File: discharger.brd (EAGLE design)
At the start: 35.6 x 61 mm, 73 parts, among them U1 BW6101, U10 BW6101, U11 BW6101, U12 BW6101, U2 BW6101, U3 BW6101, U4 BW6101, U5 BW6101, U6 BW6101, U7 BW6101, U8 BW6101, U9 BW6101

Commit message: more layout, update pdf
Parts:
- added C1, C10, C11, C12, C2, C3, C4, C5, C6, C7, C8, C9: 0.1uF, resistor:C0603
- R12, R15, R18, R21, R24, R27, R3, R30, R33, R36, R6, R9: device resistor:R0805W -> resistor:R0603
- moved R24 1.83 mm to (8.64, 36.3), turned to 270 degrees
- moved R15 1.83 mm to (8.64, 22.6), turned to 270 degrees
- moved R18 1.83 mm to (8.64, 27.2), turned to 270 degrees
- moved R6 1.83 mm to (8.64, 8.89), turned to 270 degrees
- moved R9 1.83 mm to (8.64, 13.5), turned to 270 degrees
- moved R3 1.83 mm to (8.64, 4.32), turned to 270 degrees
- moved R12 1.83 mm to (8.64, 18.0), turned to 270 degrees
- moved R21 1.83 mm to (8.64, 31.8), turned to 270 degrees
- moved R27 1.83 mm to (8.64, 40.9), turned to 270 degrees
- moved R30 1.83 mm to (8.64, 45.5), turned to 270 degrees
- moved R33 1.83 mm to (8.64, 50.0), turned to 270 degrees
- moved R36 1.83 mm to (8.64, 54.6), turned to 270 degrees
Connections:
- net B-: now also C1.2
- net B1: now also C1.1, C2.2
- net B10: now also C10.1, C11.2
- net B11: now also C11.1, C12.2
- net B12: now also C12.1
- net B2: now also C2.1, C3.2
- net B3: now also C3.1, C4.2
- net B4: now also C4.1, C5.2
- net B5: now also C5.1, C6.2
- net B6: now also C6.1, C7.2
- net B7: now also C7.1, C8.2
- net B8: now also C8.1, C9.2
- net B9: now also C10.2, C9.1
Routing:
- net B2: track 89.6 -> 104.1 mm
- net B4: track 80.0 -> 94.0 mm
- net B6: track 73.4 -> 83.7 mm
- net B3: track 85.3 -> 94.3 mm
- net B7: track 67.0 -> 76.0 mm
- net B1: track 95.5 -> 104.5 mm
- net B11: track 44.4 -> 53.2 mm
- net B5: track 76.3 -> 85.1 mm
- net B9: track 58.6 -> 67.4 mm
- net B8: track 66.8 -> 73.5 mm
- net B10: track 60.2 -> 63.3 mm
- net B-: track 98.5 -> 101.5 mm
- net B12: track 17.4 -> 14.6 mm, vias 1 -> 0
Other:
- board text added: "B-"
- board text added: "B1"
- board text added: "B10"
- board text added: "B11"
- board text added: "B12"
- board text added: "B2"
- board text added: "B3"
- board text added: "B4"
- board text added: "B5"
- board text added: "B6"
- board text added: "B7"
- board text added: "B8"
- board text added: "B9"
- board text added: "BW6101 Discharger"

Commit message: layout tweaks
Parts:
- LED1, LED10, LED11, LED12, LED2, LED3, LED4, LED5, LED6, LED7, LED8, LED9: device led:CHIP-LED0805 -> led:CHIP-LED0603
- R1, R10, R16, R19, R22, R25, R28, R31, R34, R4, R7: device resistor:R0805W -> resistor:R0603
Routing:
- net N$85: track 2.98 -> 3.48 mm
- net N$75: track 2.98 -> 3.48 mm
- net N$65: track 2.98 -> 3.48 mm
- net N$60: track 2.98 -> 3.48 mm
- net N$50: track 2.98 -> 3.48 mm
- net N$45: track 2.98 -> 3.48 mm
- net N$30: track 2.98 -> 3.48 mm
- net N$25: track 2.98 -> 3.48 mm
- net N$20: track 2.98 -> 3.48 mm
- net N$15: track 2.98 -> 3.48 mm
- net N$10: track 2.98 -> 3.48 mm

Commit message: tweaks
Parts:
- C1, C10, C11, C12, C2, C3, C4, C5, C6, C7, C8, C9: device resistor:C0603 -> resistor:C0805
- LED1, LED10, LED11, LED12, LED2, LED3, LED4, LED5, LED6, LED7, LED8, LED9: device led:CHIP-LED0603 -> led:CHIP-LED0805
- R1, R10, R12, R15, R16, R18, R19, R21, R22, R24, R25, R27, R28, R3, R30, R31, R33, R34, R36, R4, R6, R7, R9: device resistor:R0603 -> resistor:R0805
- R13: device resistor:R0805W -> resistor:R0805
- moved R12 0.25 mm to (8.38, 18.0)
- moved R15 0.25 mm to (8.38, 22.6)
- moved R18 0.25 mm to (8.38, 27.2)
- moved R21 0.25 mm to (8.38, 31.8)
- moved R24 0.25 mm to (8.38, 36.3)
- moved R27 0.25 mm to (8.38, 40.9)
- moved R3 0.25 mm to (8.38, 4.32)
- moved R30 0.25 mm to (8.38, 45.5)
- moved R33 0.25 mm to (8.38, 50.0)
- moved R36 0.25 mm to (8.38, 54.6)
- moved R6 0.25 mm to (8.38, 8.89)
- moved R9 0.25 mm to (8.38, 13.5)

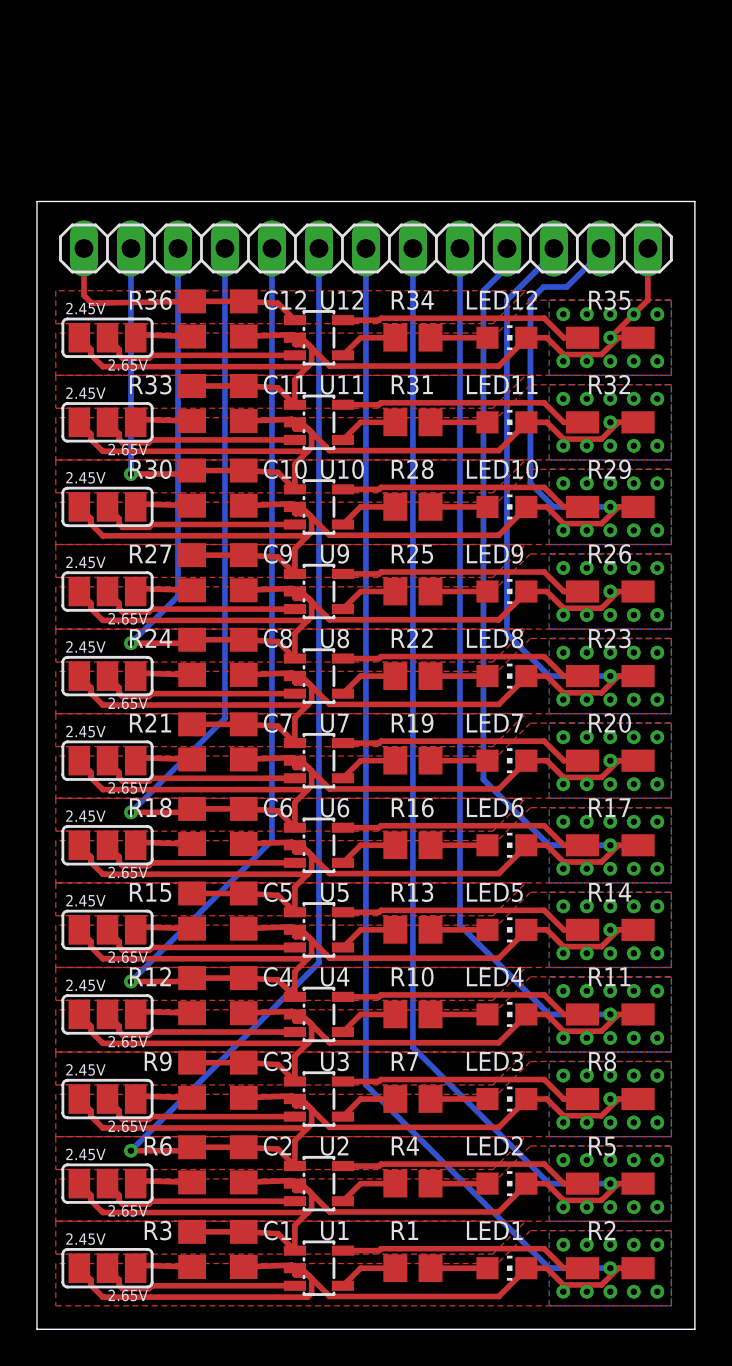
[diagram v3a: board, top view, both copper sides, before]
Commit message: use 2512 resistors to dissipate more power
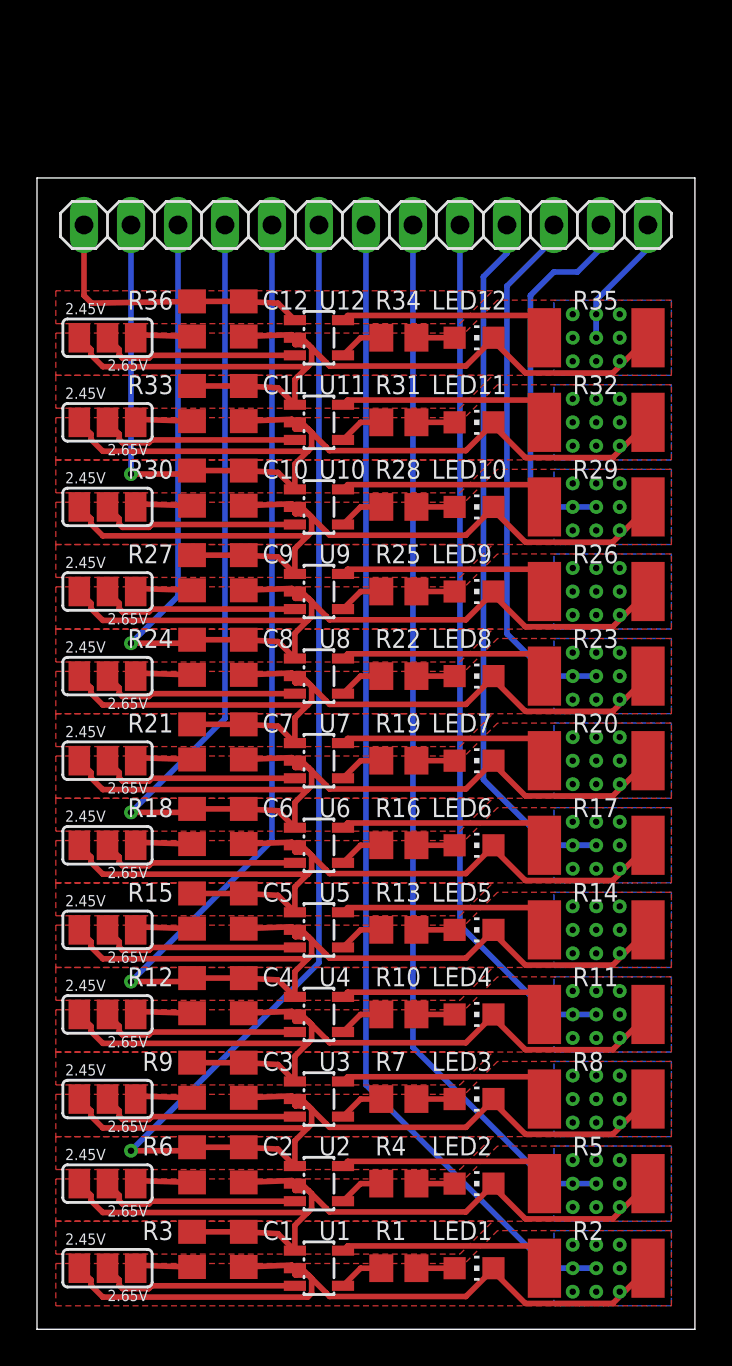
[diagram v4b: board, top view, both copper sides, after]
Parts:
- R11, R14, R17, R2, R20, R23, R26, R29, R32, R35, R5, R8: device resistor:R1206W -> resistor:R2512
- moved LED1 1.78 mm to (23.6, 3.30)
- moved LED10 1.78 mm to (23.6, 44.5)
- moved LED11 1.78 mm to (23.6, 49.0)
- moved LED12 1.78 mm to (23.6, 53.6)
- moved LED2 1.78 mm to (23.6, 7.87)
- moved LED3 1.78 mm to (23.6, 12.4)
- moved LED4 1.78 mm to (23.6, 17.0)
- moved LED5 1.78 mm to (23.6, 21.6)
- moved LED6 1.78 mm to (23.6, 26.2)
- moved LED7 1.78 mm to (23.6, 30.7)
- moved LED8 1.78 mm to (23.6, 35.3)
- moved LED9 1.78 mm to (23.6, 39.9)
- moved JP1 1.27 mm to (17.8, 59.7)
- moved R1 0.76 mm to (19.6, 3.30)
- moved R10 0.76 mm to (19.6, 17.0)
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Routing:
- net B11: track 53.5 -> 56.6 mm, vias 11 -> 9
- net B4: track 94.0 -> 96.8 mm, vias 12 -> 10
- net B6: track 83.8 -> 86.6 mm, vias 12 -> 10
- net B2: track 104.2 -> 107.0 mm, vias 12 -> 10
- net B10: track 63.5 -> 66.2 mm, vias 12 -> 10
- net B8: track 73.6 -> 76.4 mm, vias 12 -> 10
- net B9: track 67.7 -> 69.7 mm, vias 11 -> 9
- net B7: track 76.3 -> 78.2 mm, vias 11 -> 9
- net B5: track 85.4 -> 87.4 mm, vias 11 -> 9
- net B1: track 104.7 -> 106.7 mm, vias 11 -> 9
- net B-: track 101.5 -> 103.5 mm, vias 11 -> 9
- net B3: track 94.5 -> 96.5 mm, vias 11 -> 9
- net N$21: track 13.4 -> 11.8 mm
- net N$81: track 13.4 -> 11.8 mm
- net N$71: track 13.4 -> 11.8 mm
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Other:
- board size 35.6 x 61 mm -> 35.6 x 62.2 mm

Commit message: bump version, minor changes
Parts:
- LED1, LED10, LED11, LED12, LED2, LED3, LED4, LED5, LED6, LED7, LED8, LED9: device led:CHIP-LED0805 -> led:SML0805
- turned LED1 to 180 degrees
- turned LED10 to 180 degrees
- turned LED11 to 180 degrees
- turned LED12 to 180 degrees
- turned LED2 to 180 degrees
- turned LED3 to 180 degrees
- turned LED4 to 180 degrees
- turned LED5 to 180 degrees
- turned LED6 to 180 degrees
- turned LED7 to 180 degrees
- turned LED8 to 180 degrees
- turned LED9 to 180 degrees

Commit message: updates
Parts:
- added LED13, LED14, LED15, LED16, LED17, LED18, LED19, LED20, LED21, LED22, LED23, LED24: ALARM, led:SML0805
- added R37, R38, R39, R40, R41, R42, R43, R44, R45, R46, R47, R48: 1K, resistor:R0805
- C1, C10, C11, C12, C2, C3, C4, C5, C6, C7, C8, C9: device resistor:C0805 -> resistor:C0603
- LED1, LED10, LED11, LED12, LED2, LED3, LED4, LED5, LED6, LED7, LED8, LED9: value ALARM -> BLEED
- R1, R10, R4, R7: value 100R -> 47R; device resistor:R0805 -> resistor:R2512
- R12, R3, R6, R9: value 1K -> 47R; device resistor:R0805 -> resistor:R2512
- R14, R17, R20, R23, R26, R29, R32, R35: value 47R -> 100R; device resistor:R2512 -> resistor:R0805
- R15, R18, R21, R24, R27, R30, R33, R36: value 1K -> 100R
- moved R12 47.1 mm to (30.7, 59.4), turned to 0 degrees
- moved R9 38.0 mm to (30.7, 44.2), turned to 0 degrees
- moved R11 37.3 mm to (30.7, 54.4)
- moved R25 37.3 mm to (19.3, 2.54)
- moved R10 34.1 mm to (30.7, 49.3)
- moved R26 34.1 mm to (19.3, 7.62)
- moved R27 30.2 mm to (19.3, 12.7), turned to 0 degrees
- moved R6 30.0 mm to (30.7, 29.0), turned to 0 degrees
- moved R8 26.7 mm to (30.7, 39.1)
- moved R28 26.7 mm to (19.3, 17.8)
- moved R24 26.5 mm to (19.3, 60.5), turned to 0 degrees
- moved R7 24.3 mm to (30.7, 34.0)
- moved R3 24.2 mm to (30.7, 13.7), turned to 0 degrees
- moved R29 24.2 mm to (19.3, 22.9)
- moved R23 22.8 mm to (19.3, 55.4)
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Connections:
- new net N$1: R1.1, R13.1, U1.5
- new net N$2: LED1.A, R13.2
- new net N$3: R25.1, U1.4
- new net N$31: LED10.A, R22.2
- new net N$32: LED11.A, R23.2
- new net N$33: LED12.A, R24.2
- new net N$34: LED6.A, R18.2
- new net N$35: LED5.A, R17.2
- new net N$4: LED2.A, R14.2
- new net N$51: LED4.A, R16.2
- new net N$52: LED3.A, R15.2
- new net N$60: LED19.A, R31.2
- net B-: now also LED13.C, R1.2; no longer R2.2
- net B1: now also LED14.C, R2.2, R37.1; no longer R3.1, R5.2
- net B10: now also LED23.C, R11.2, R46.1; no longer R30.1, R32.2
- net B11: now also LED24.C, R12.2, R47.1; no longer R33.1, R35.2
- net B12: now also R48.1; no longer R36.1
- net B2: now also LED15.C, R3.2, R38.1; no longer R6.1, R8.2
- net B3: now also LED16.C, R39.1, R4.2; no longer R11.2, R9.1
- net B4: now also LED17.C, R40.1, R5.2; no longer R12.1, R14.2
- net B5: now also LED18.C, R41.1, R6.2; no longer R15.1, R17.2
- net B6: now also LED19.C, R42.1, R7.2; no longer R18.1, R20.2
- net B7: now also LED20.C, R43.1, R8.2; no longer R21.1, R23.2
- net B8: now also LED21.C, R44.1, R9.2; no longer R24.1, R26.2
- net B9: now also LED22.C, R10.2, R45.1; no longer R27.1, R29.2
- net N$10: now also LED15.A, R27.2; no longer LED3.A, R7.2
- net N$11: now also LED8.A, R20.2; no longer R2.1, U1.5
- net N$13: now also R37.2; no longer R3.2
- net N$14: now also LED9.A, R21.2; no longer R1.1, U1.4
- net N$15: now also LED13.A, R25.2; no longer LED1.A, R1.2
- net N$16: now also R20.1, R8.1; no longer R23.1
- net N$18: now also R44.2; no longer R24.2
- net N$19: now also R32.1; no longer R22.1
- net N$20: now also LED20.A, R32.2; no longer LED8.A, R22.2
- net N$21: now also R14.1, R2.1; no longer R5.1
- net N$23: now also R38.2; no longer R6.2
- net N$24: now also R26.1; no longer R4.1
- net N$25: now also LED14.A, R26.2; no longer LED2.A, R4.2
- net N$26: now also R16.1, R4.1; no longer R11.1
- net N$28: now also R40.2; no longer R12.2
- net N$29: now also R28.1; no longer R10.1
- net N$30: now also LED16.A, R28.2; no longer LED4.A, R10.2
- net N$36: now also R17.1, R5.1; no longer R14.1
- net N$38: now also R41.2; no longer R15.2
- net N$39: now also R29.1; no longer R13.1
- net N$40: now also LED17.A, R29.2; no longer LED5.A, R13.2
- net N$41: now also R21.1, R9.1; no longer R26.1
- net N$43: now also R45.2; no longer R27.2
- net N$44: now also R33.1; no longer R25.1
- net N$45: now also LED21.A, R33.2; no longer LED9.A, R25.2
- net N$46: now also R18.1, R6.1; no longer R17.1
- net N$48: now also R42.2; no longer R18.2
- net N$49: now also R30.1; no longer R16.1
- net N$50: now also LED18.A, R30.2; no longer LED6.A, R16.2
- net N$56: now also R19.1, R7.1; no longer R20.1
- net N$58: now also R43.2; no longer R21.2
- net N$59: now also R31.1; no longer R19.1
- net N$6: now also R15.1, R3.1; no longer R8.1
- net N$61: now also R10.1, R22.1; no longer R29.1
- net N$63: now also R46.2; no longer R30.2
- net N$64: now also R34.1; no longer R28.1
- net N$65: now also LED22.A, R34.2; no longer LED10.A, R28.2
- net N$71: now also R11.1, R23.1; no longer R32.1
- net N$73: now also R47.2; no longer R33.2
- net N$74: now also R35.1; no longer R31.1
- net N$75: now also LED23.A, R35.2; no longer LED11.A, R31.2
- net N$8: now also R39.2; no longer R9.2
- net N$81: now also R12.1, R24.1; no longer R35.1
- net N$83: now also R48.2; no longer R36.2
- net N$84: now also R36.1; no longer R34.1
- net N$85: now also LED24.A, R36.2; no longer LED12.A, R34.2
- net N$9: now also R27.1; no longer R7.1
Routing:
- net N$1: track 0.00 -> 17.7 mm
- net N$11: track 11.8 -> 2.57 mm
- net B-: track 103.5 -> 112.0 mm
- net N$41: track 11.8 -> 17.7 mm
- net N$26: track 11.8 -> 17.7 mm
- net N$46: track 11.8 -> 17.7 mm
- net N$56: track 11.8 -> 17.7 mm
- net N$71: track 11.8 -> 17.7 mm
- net N$36: track 11.8 -> 17.7 mm
- net N$21: track 11.8 -> 17.7 mm
- net N$6: track 11.8 -> 17.7 mm
- net N$61: track 11.8 -> 17.7 mm
- net N$16: track 11.8 -> 17.7 mm
- net N$81: track 11.8 -> 17.7 mm
- net B2: track 107.0 -> 101.5 mm
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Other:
- board size 35.6 x 62.2 mm -> 35.6 x 69.8 mm

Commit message: move 1k resistor onto SEL side of jumper
more fiddling
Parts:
- R13, R14, R15, R16, R17, R18, R19, R20, R21, R22, R23, R24, R25, R26, R27, R28, R29, R30, R31, R32, R33, R34, R35, R36: device resistor:R0805 -> resistor:R0603
- moved R37 0.57 mm to (5.59, 3.30), turned to 0 degrees
- moved R43 0.51 mm to (5.59, 33.8), turned to 0 degrees
- moved R45 0.51 mm to (5.59, 43.9), turned to 0 degrees
- moved R46 0.51 mm to (5.59, 49.0), turned to 0 degrees
- moved R47 0.51 mm to (5.59, 54.1), turned to 0 degrees
- moved R38 0.51 mm to (5.59, 8.38), turned to 0 degrees
- moved R39 0.51 mm to (5.59, 13.5), turned to 0 degrees
- moved R40 0.51 mm to (5.59, 18.5), turned to 0 degrees
- moved R41 0.51 mm to (5.59, 23.6), turned to 0 degrees
- moved R42 0.51 mm to (5.59, 28.7), turned to 0 degrees
- moved R44 0.51 mm to (5.59, 38.9), turned to 0 degrees
- moved R48 0.51 mm to (5.59, 59.2), turned to 0 degrees
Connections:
- removed net N$72: SJ11.2, U11.3
- removed net N$73: R47.2, SJ11.3
- removed net N$82: SJ12.2, U12.3
- removed net N$83: R48.2, SJ12.3
- new net N$53: R44.2, U8.3
- new net N$54: R43.2, U7.3
- new net N$55: R42.2, U6.3
- new net N$66: R37.2, U1.3
- net B1: now also SJ1.3; no longer R37.1
- net B10: now also SJ10.3; no longer R46.1
- net B11: now also SJ11.3; no longer R47.1
- net B12: now also SJ12.3; no longer R48.1
- net B2: now also SJ2.3; no longer R38.1
- net B3: now also SJ3.3; no longer R39.1
- net B4: now also SJ4.3; no longer R40.1
- net B5: now also SJ5.3; no longer R41.1
- net B6: now also SJ6.3; no longer R42.1
- net B7: now also SJ7.3; no longer R43.1
- net B8: now also SJ8.3; no longer R44.1
- net B9: now also SJ9.3; no longer R45.1
- net N$12: now also R39.1, SJ3.2; no longer SJ1.2, U1.3
- net N$13: now also R40.1, SJ4.2; no longer R37.2, SJ1.3
- net N$17: now also R41.1, SJ5.2; no longer SJ8.2, U8.3
- net N$18: now also R42.1, SJ6.2; no longer R44.2, SJ8.3
- net N$22: now also R43.1, SJ7.2; no longer SJ2.2, U2.3
- net N$23: now also R44.1, SJ8.2; no longer R38.2, SJ2.3
- net N$27: now also R45.1, SJ9.2; no longer SJ4.2, U4.3
- net N$28: now also R46.1, SJ10.2; no longer R40.2, SJ4.3
- net N$37: now also R47.1, SJ11.2; no longer SJ5.2, U5.3
- net N$38: now also R48.1, SJ12.2; no longer R41.2, SJ5.3
- net N$42: now also R48.2, U12.3; no longer SJ9.2, U9.3
- net N$43: now also R47.2, U11.3; no longer R45.2, SJ9.3
- net N$47: now also R46.2, U10.3; no longer SJ6.2, U6.3
- net N$48: now also R45.2, U9.3; no longer R42.2, SJ6.3
- net N$57: now also R41.2, U5.3; no longer SJ7.2, U7.3
- net N$58: now also R40.2, U4.3; no longer R43.2, SJ7.3
- net N$62: now also R39.2, U3.3; no longer SJ10.2, U10.3
- net N$63: now also R38.2, U2.3; no longer R46.2, SJ10.3
- net N$7: now also R37.1, SJ1.2; no longer SJ3.2, U3.3
- net N$8: now also R38.1, SJ2.2; no longer R39.2, SJ3.3
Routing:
- net B3: track 98.9 -> 114.0 mm
- net B5: track 88.7 -> 103.3 mm
- net B1: track 110.0 -> 124.6 mm
- net B7: track 78.5 -> 92.8 mm
- net B9: track 68.4 -> 82.2 mm
- net B11: track 54.4 -> 68.2 mm
- net B4: track 91.3 -> 104.9 mm
- net B6: track 81.2 -> 94.7 mm
- net B10: track 60.8 -> 74.3 mm
- net N$82: track 11.4 -> 0.00 mm
- net N$72: track 11.4 -> 0.00 mm
- net B8: track 71.0 -> 81.4 mm
- net N$17: track 11.4 -> 2.61 mm
- net N$27: track 11.4 -> 2.61 mm
- net N$37: track 11.4 -> 2.61 mm
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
